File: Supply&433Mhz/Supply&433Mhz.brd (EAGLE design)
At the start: 65 x 56.5 mm, 17 parts, among them K1 61004021821, P1 DF11-06-2DS, Q1 BS170

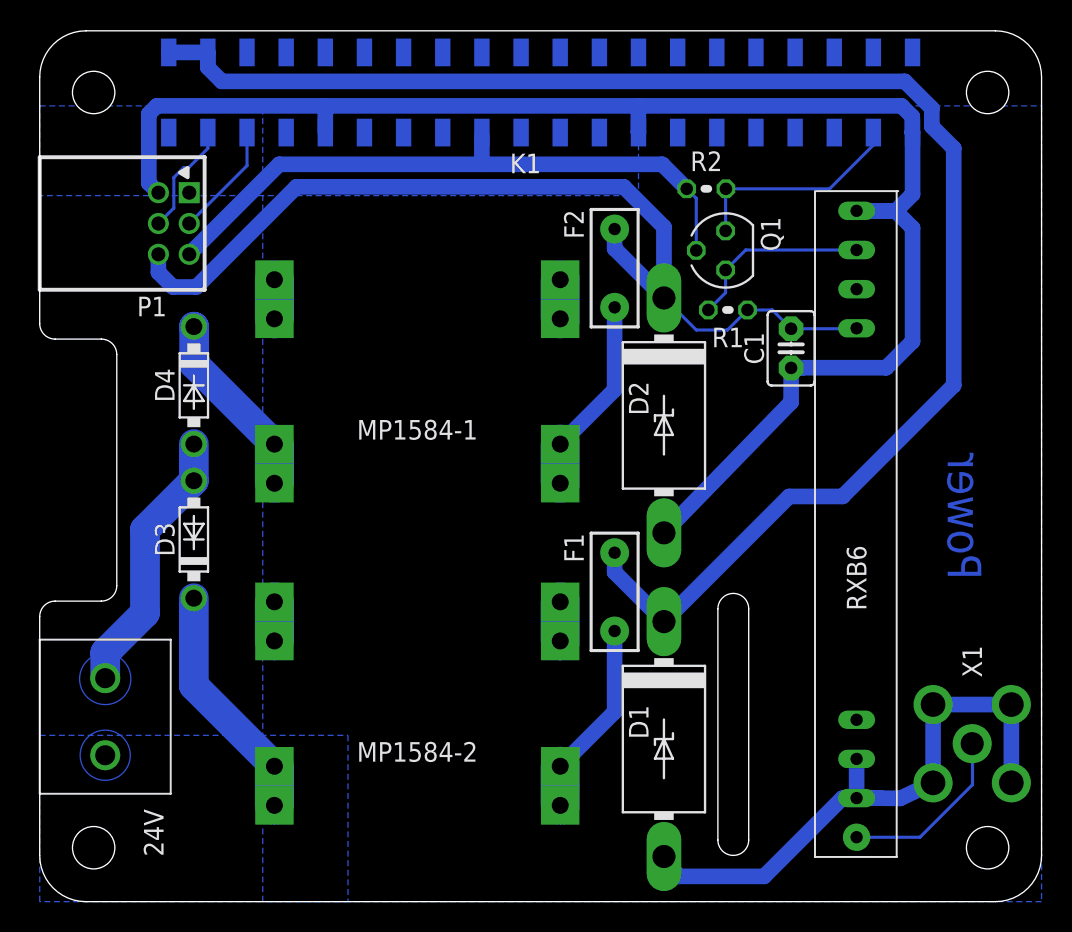
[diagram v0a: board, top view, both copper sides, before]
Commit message: Remove pull-up to 5V since level-shifter worked not properly. Use 10K instead of 1K resistor as pull-up to 3.3V.
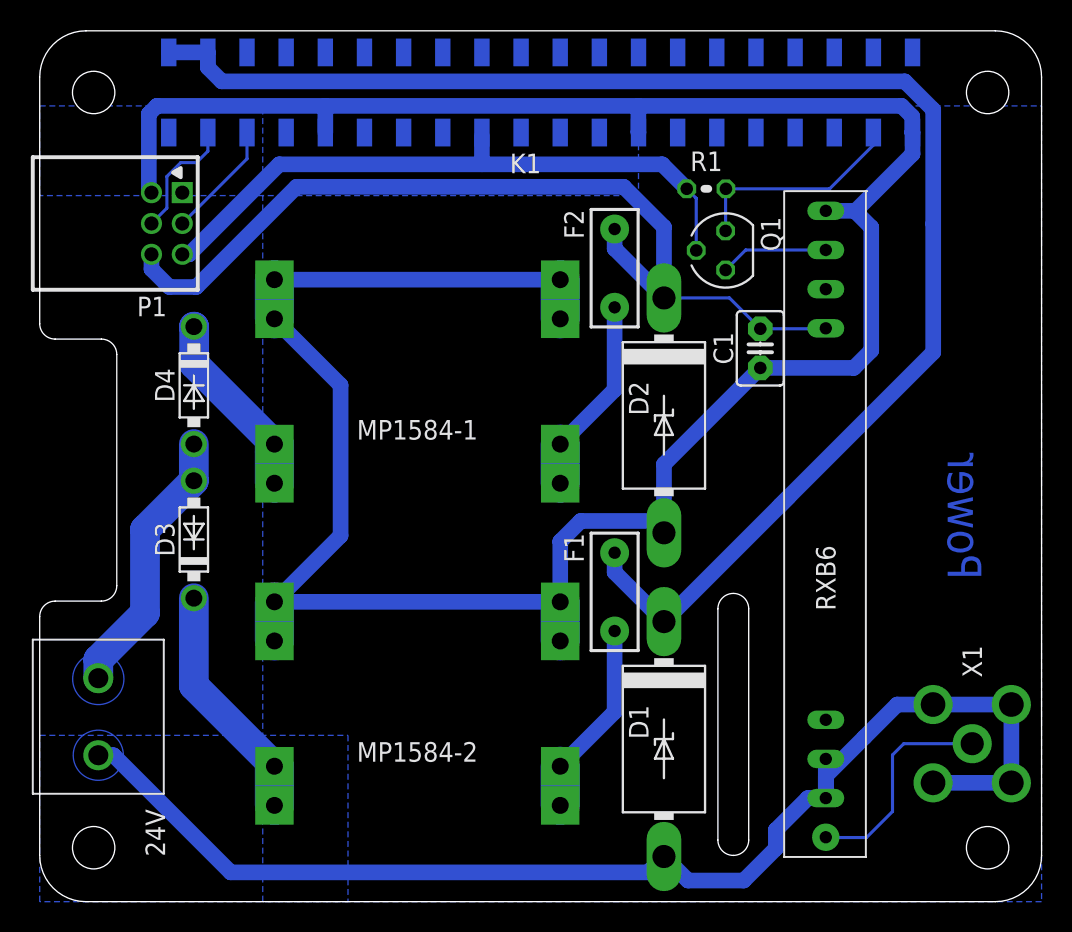
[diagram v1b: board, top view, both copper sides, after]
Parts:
- removed R2: 1K, rcl:0204V
- R1: value 1K -> 10K
- moved R1 7.98 mm to (43.2, 46.2)
- moved C1 2.00 mm to (46.8, 35.9)
- moved RXB6 2.00 mm to (51.0, 24.5)
- moved 24V 0.45 mm to (3.80, 12.0)
- moved P1 0.45 mm to (8.25, 44.0)
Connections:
- net N$11: now also R1.2; no longer R2.2
- net N$2: no longer R1.1
- net N$3: no longer R1.2
- net N$69: now also R1.1; no longer R2.1
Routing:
- net GND: track 152.0 -> 264.4 mm
- net N$3: track 12.1 -> 7.04 mm
- net N$2: track 63.0 -> 60.2 mm
- net N$8: track 11.6 -> 14.2 mm
- net N$5: track 101.1 -> 98.8 mm
- net N$12: track 7.42 -> 8.01 mm

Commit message: Increase RXB6 drills. Change some wires.
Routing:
- net N$8: track 14.2 -> 12.0 mm
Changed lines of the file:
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@@
 <contactref element="R1" pad="1"/>
 <contactref element="K1" pad="19"/>
-<wire x1="54.09" y1="49.09" x2="54.09" y2="49.9" width="0.2032" layer="16"/>
 <wire x1="44.52" y1="46.25" x2="44.5" y2="46.23" width="0.2032" layer="16"/>
 <wire x1="44.5" y1="46.23" x2="44.5" y2="43.52" width="0.2032" layer="16"/>
-<wire x1="54.09" y1="49.09" x2="51.25" y2="46.25" width="0.2032" layer="16"/>
-<wire x1="51.25" y1="46.25" x2="44.52" y2="46.25" width="0.2032" layer="16"/>
+<wire x1="54.09" y1="49.9" x2="54.09" y2="48.81" width="0.2032" layer="16"/>
+<wire x1="54.09" y1="48.81" x2="53.17" y2="47.89" width="0.2032" layer="16"/>
+<wire x1="53.17" y1="47.89" x2="46.16" y2="47.89" width="0.2032" layer="16"/>
+<wire x1="46.16" y1="47.89" x2="44.52" y2="46.25" width="0.2032" layer="16"/>
 </signal>
 <signal name="N$3">
@@
 <contactref element="X1" pad="ANTENNA"/>
 <contactref element="RXB6" pad="ANT"/>
-<wire x1="60.5" y1="10.25" x2="56.06" y2="10.25" width="0.2032" layer="16"/>
-<wire x1="56.06" y1="10.25" x2="55.33" y2="9.52" width="0.2032" layer="16"/>
-<wire x1="55.33" y1="9.52" x2="55.33" y2="5.85" width="0.2032" layer="16"/>
-<wire x1="55.33" y1="5.85" x2="53.64" y2="4.16" width="0.2032" layer="16"/>
-<wire x1="53.64" y1="4.16" x2="51.02" y2="4.16" width="0.2032" layer="16"/>
-<wire x1="51.02" y1="4.16" x2="51" y2="4.18" width="0.2032" layer="16"/>
+<wire x1="51.02" y1="4.16" x2="51.4" y2="4.16" width="0.2032" layer="16"/>
+<wire x1="51.4" y1="4.16" x2="55.34" y2="8.1" width="0.2032" layer="16"/>
+<wire x1="55.34" y1="8.1" x2="57.49" y2="10.25" width="0.2032" layer="16"/>
+<wire x1="57.49" y1="10.25" x2="60.5" y2="10.25" width="0.2032" layer="16"/>
+<wire x1="51.02" y1="4.16" x2="51" y2="4.18" width="0" layer="19" extent="16-16"/>
 </signal>
 </signals>

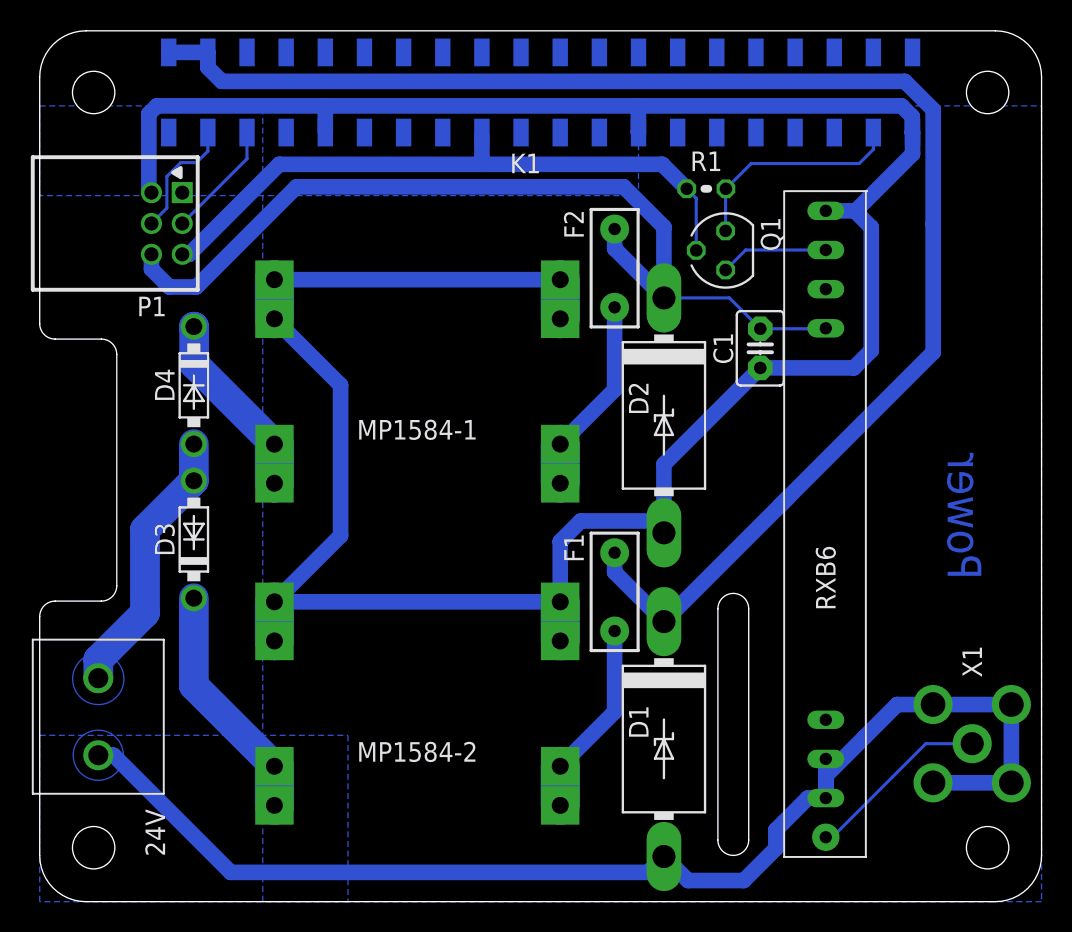
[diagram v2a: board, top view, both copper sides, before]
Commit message: Use external 3.3V supply instead of raspberry one.
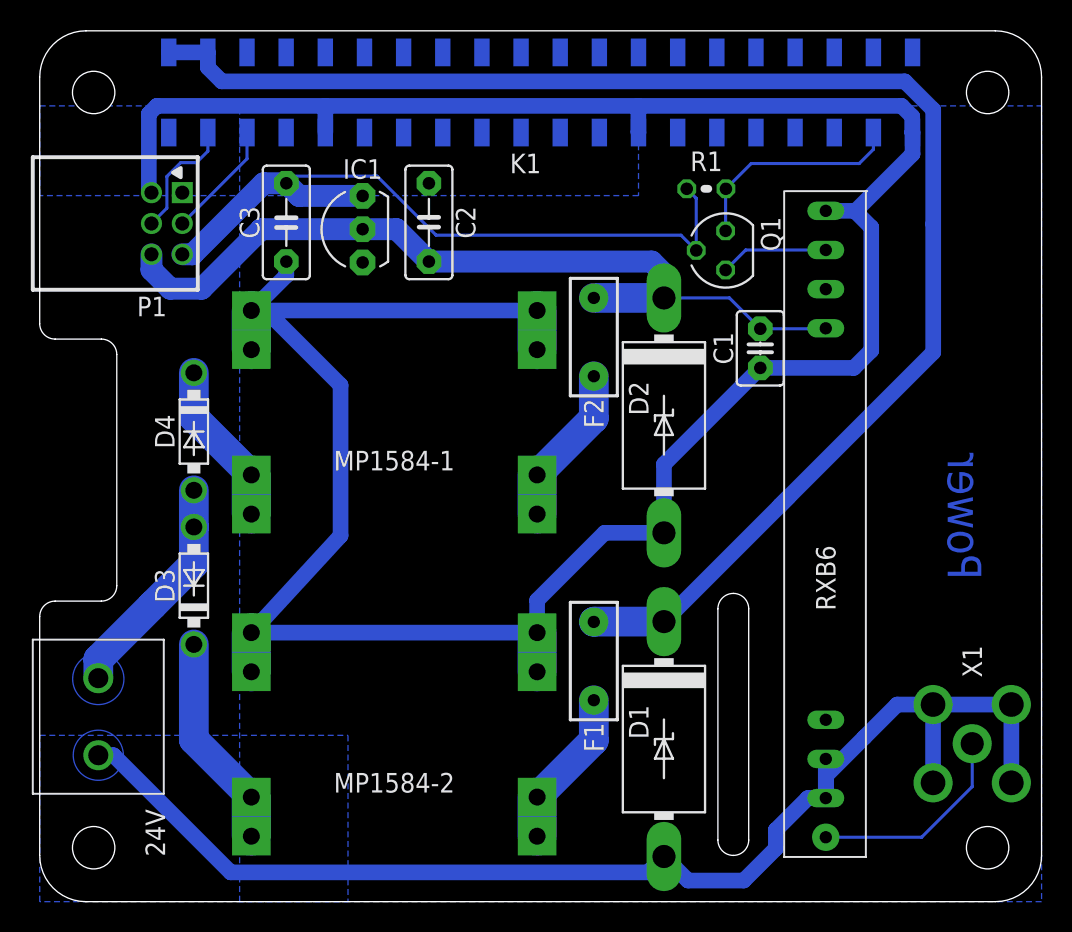
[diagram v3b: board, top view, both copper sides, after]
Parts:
- added C2, C3: 1uF, capacitor-wima:C5B3
- added IC1: 3.3V, adafruit:TO92-INLINE
- moved F1 4.69 mm to (36.0, 15.6)
- moved F2 4.67 mm to (36.0, 36.6)
- moved D3 3.00 mm to (10.0, 20.5)
- moved D4 3.00 mm to (10.0, 30.5)
- moved MP1584-1 2.50 mm to (23.0, 31.8)
- moved MP1584-2 2.50 mm to (23.0, 10.8)
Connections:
- net GND: now also C2.2, C3.2, IC1.1
- net N$11: now also C3.1, IC1.3; no longer K1.9
- net N$2: now also C2.1, IC1.2
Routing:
- net GND: track 264.4 -> 270.6 mm
- net N$2: track 60.2 -> 55.0 mm
- net N$11: track 42.4 -> 47.0 mm
- net +24V: track 17.8 -> 14.8 mm
- net N$4: track 12.8 -> 10.3 mm
- net N$6: track 12.9 -> 10.5 mm
- net N$9: track 12.9 -> 10.7 mm
- net N$8: track 12.0 -> 13.6 mm
- net N$7: track 15.6 -> 14.0 mm
- net N$5: track 98.8 -> 97.5 mm

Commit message: Minor.
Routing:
- net N$5: track 97.5 -> 96.7 mm
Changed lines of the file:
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@@
 <wire x1="19.52" y1="23.745" x2="13.729" y2="17.454" width="1.016" layer="16"/>
 <wire x1="51" y1="6.72" x2="51" y2="8.16" width="1.016" layer="16"/>
-<wire x1="51" y1="8.16" x2="53.51" y2="10.67" width="1.016" layer="16"/>
-<wire x1="53.51" y1="10.67" x2="55.63" y2="12.79" width="1.016" layer="16"/>
+<wire x1="51" y1="8.16" x2="55.63" y2="12.79" width="1.016" layer="16"/>
 <wire x1="55.63" y1="12.79" x2="57.96" y2="12.79" width="1.016" layer="16"/>
 <wire x1="56.63" y1="49.9" x2="56.63" y2="48.51" width="1.016" layer="16"/>
@@
 <wire x1="10" y1="26.69" x2="10" y2="24.31" width="1.9304" layer="16"/>
 <wire x1="10" y1="24.31" x2="10" y2="21.92" width="1.9304" layer="16"/>
-<wire x1="10" y1="21.92" x2="7.32" y2="19.24" width="1.9304" layer="16"/>
-<wire x1="7.32" y1="19.24" x2="3.8" y2="15.72" width="1.9304" layer="16"/>
+<wire x1="10" y1="21.92" x2="3.8" y2="15.72" width="1.9304" layer="16"/>
 <wire x1="3.8" y1="15.72" x2="3.8" y2="14.5" width="1.9304" layer="16"/>
 </signal>
@@
 <wire x1="48.035" y1="25.705" x2="48.62" y2="26.29" width="1.016" layer="16"/>
 <wire x1="56.13" y1="53.22" x2="57.97" y2="51.38" width="1.016" layer="16"/>
-<wire x1="57.97" y1="51.38" x2="57.97" y2="43.97" width="1.016" layer="16"/>
-<wire x1="57.97" y1="43.97" x2="57.97" y2="35.64" width="1.016" layer="16"/>
-<wire x1="57.97" y1="35.64" x2="48.035" y2="25.705" width="1.016" layer="16"/>
+<wire x1="57.97" y1="51.38" x2="57.97" y2="35.64" width="1.016" layer="16"/>
+<wire x1="57.97" y1="35.64" x2="48.62" y2="26.29" width="1.016" layer="16"/>
 <wire x1="35.95" y1="18.15" x2="35.98" y2="18.17" width="1.9304" layer="16"/>
 <wire x1="35.98" y1="18.17" x2="40.5" y2="18.17" width="1.9304" layer="16"/>
@@
 <wire x1="16.02" y1="46.61" x2="16" y2="46.61" width="0.2032" layer="16"/>
 <wire x1="16.02" y1="46.61" x2="16.48" y2="47.07" width="0.2032" layer="16"/>
-<wire x1="16.48" y1="47.07" x2="21.63" y2="47.07" width="0.2032" layer="16"/>
-<wire x1="21.63" y1="47.07" x2="21.89" y2="47.07" width="0.2032" layer="16"/>
+<wire x1="16.48" y1="47.07" x2="21.89" y2="47.07" width="0.2032" layer="16"/>
 <wire x1="21.89" y1="47.07" x2="25.72" y2="43.24" width="0.2032" layer="16"/>
 <wire x1="25.72" y1="43.24" x2="41.605" y2="43.24" width="0.2032" layer="16"/>
